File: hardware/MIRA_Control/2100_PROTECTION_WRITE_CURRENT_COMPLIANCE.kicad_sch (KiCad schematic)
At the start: 66 parts, among them U2100 ADG5408, U2101 OPA197, U2103 ADG5409, U2104 INA821, U2105 OPA4197, U2106 OPA4197, U2107 OPA4197, U2108 SN74LVC1G04, U2109 INA821

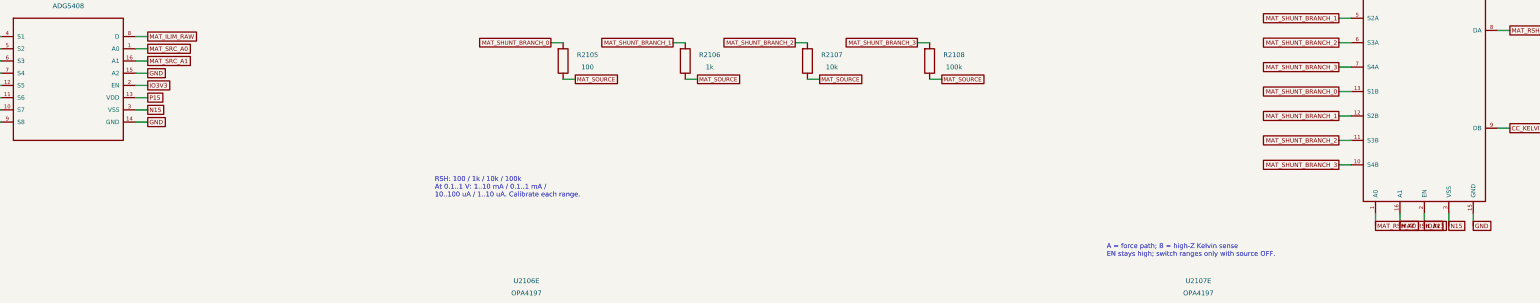
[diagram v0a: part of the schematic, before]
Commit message: Select Samtec inter-board connectors and resolve analog VSS ERC warnings
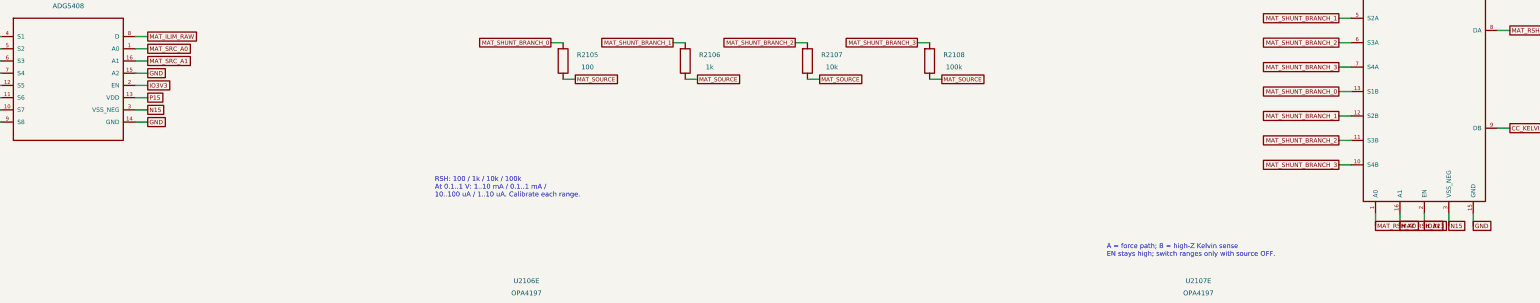
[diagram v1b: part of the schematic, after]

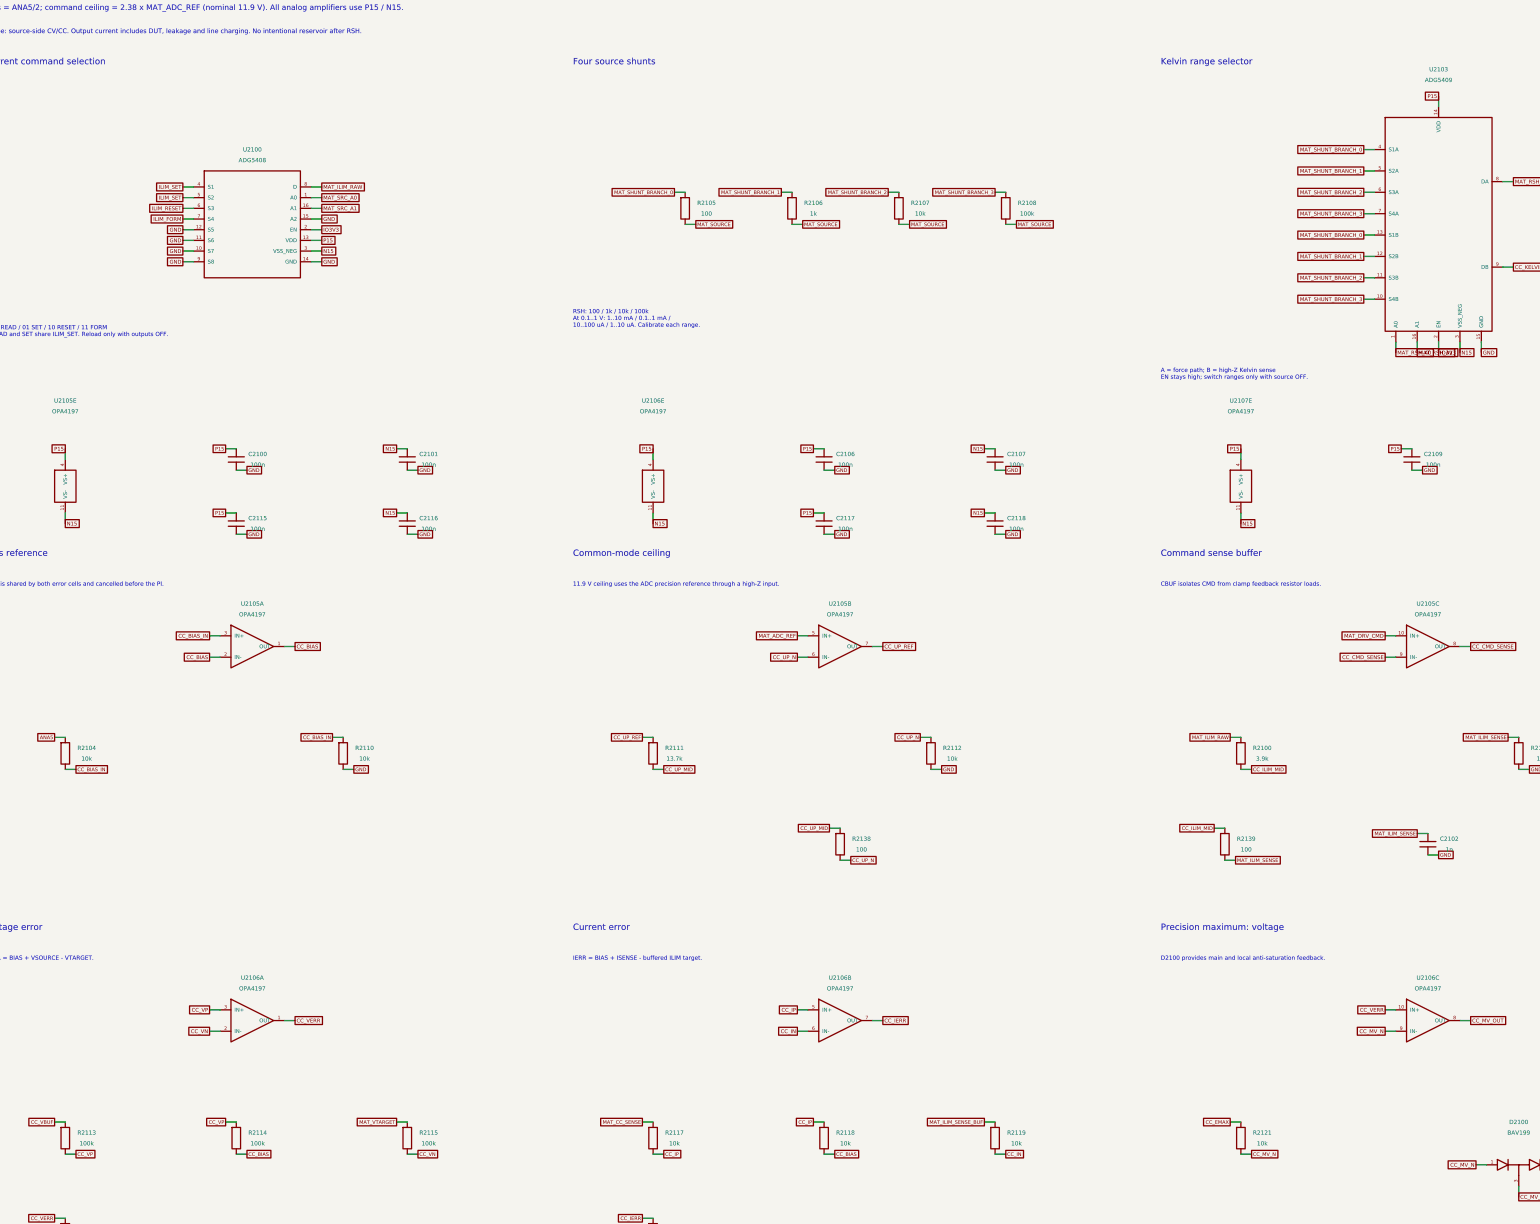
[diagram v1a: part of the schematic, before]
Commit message: Protect unpowered signal domains and qualify local supplies; retain startup and fault interlocks
MIRA-Startup-Patch: 7ffae17756ebcf923eff1212bb1aade8fbdfae03a9ca8ecebc69d3da3d3b4ba2
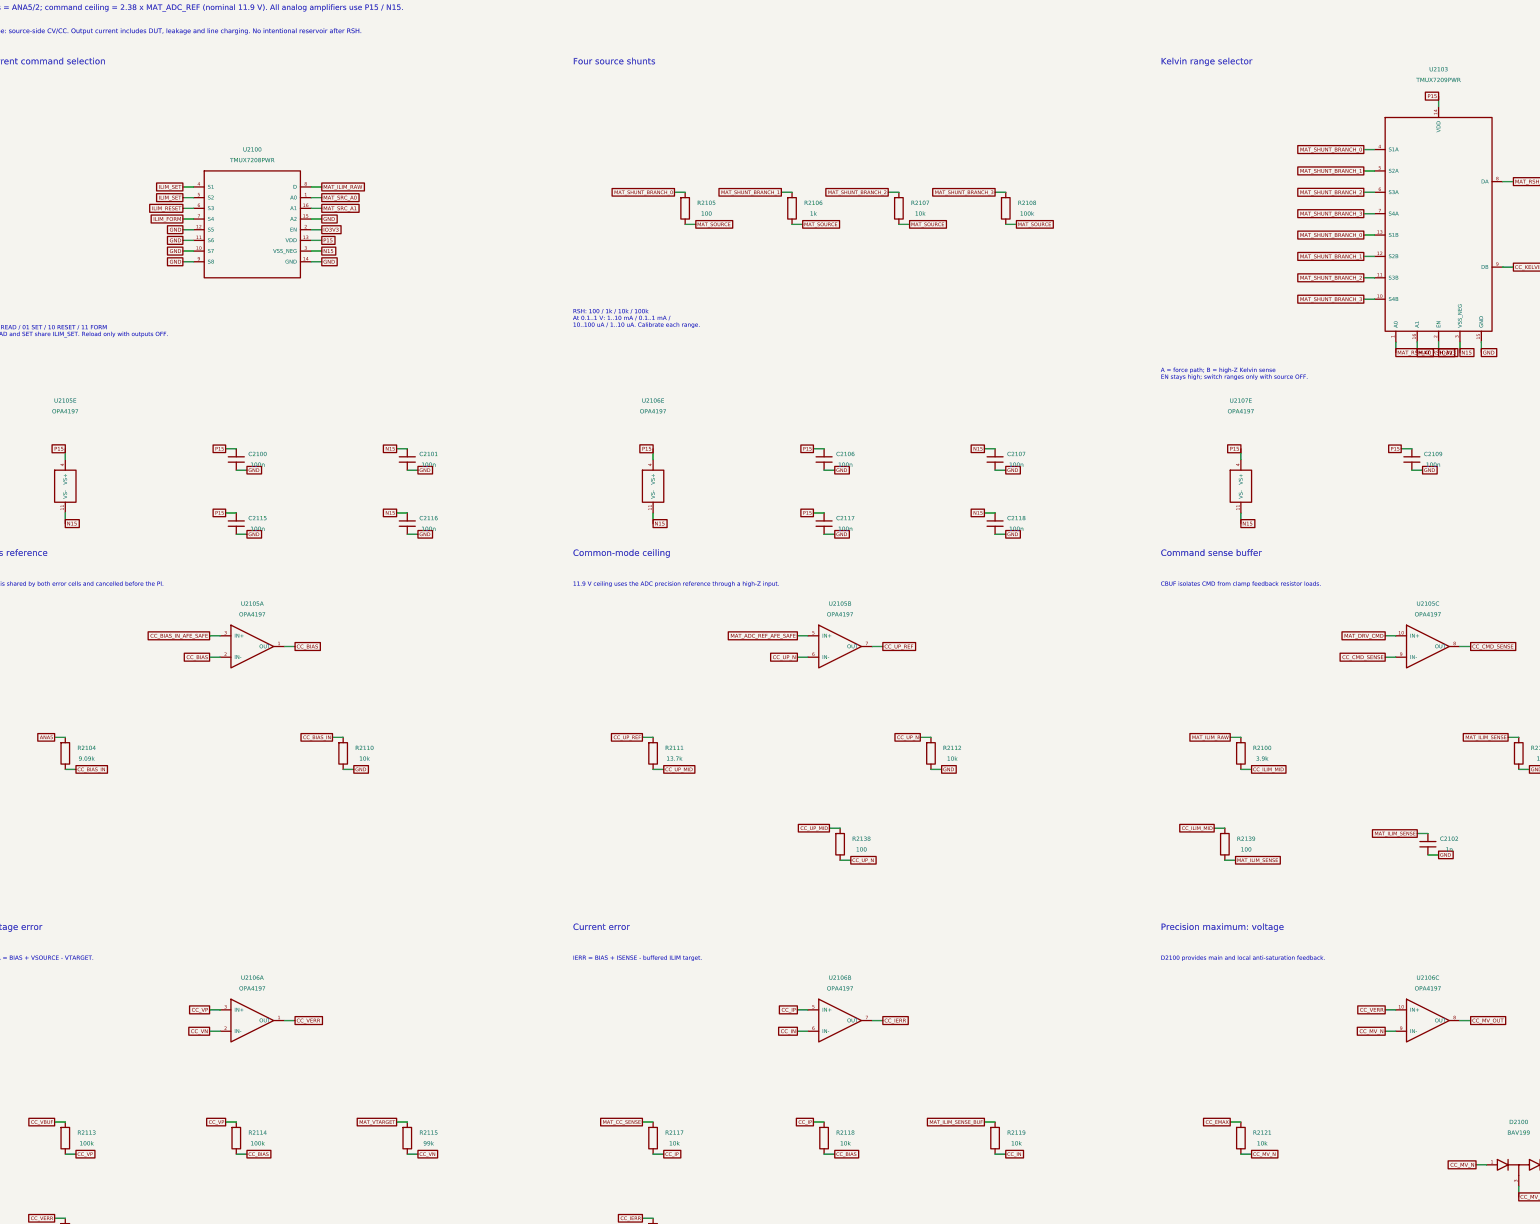
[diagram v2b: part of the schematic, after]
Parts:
- R2104: value 10k -> 9.09k; MPN RT0603BRD0710KL -> ERJ-2RKF9091X
- R2115: value 100k -> 99k; MPN RT0603BRD07100KL -> ERA-2AEB9902X
- U2100: value ADG5408 -> TMUX7208PWR; symbol MIRA_RevA:ADG5408_MIRA_MAT -> MIRA_RevA:TMUX7208PWR_SIGNAL_MIRA; MPN ADG5408BRUZ -> TMUX7208PWR; Manufacturer Analog Devices -> Texas Instruments
- U2103: value ADG5409 -> TMUX7209PWR; symbol MIRA_RevA:ADG5409_CC_MIRA -> MIRA_RevA:TMUX7209PWR_SIGNAL_MIRA; MPN ADG5409BRUZ -> TMUX7209PWR; Manufacturer Analog Devices -> Texas Instruments
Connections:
- net CC_BIAS_IN: no longer U2105.3 (IN+)
- net MAT_ADC_REF renamed MAT_ADC_REF_AFE_SAFE
- new net CC_BIAS_IN_AFE_SAFE: U2105.3 (IN+)

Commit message: MIRA.05: analog requirements and schematic fixes
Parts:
- R2104: MPN ERJ-2RKF9091X -> RT0603BRD079K09L
- R2111: value 13.7k -> 10k; MPN RT0603BRD0713K7L -> RT0603BRD0710KL
- R2115: value 99k -> 100k; MPN ERA-2AEB9902X -> RT0603BRD07100KL
- R2116: value 100k -> 101k; MPN RT0603BRD07100KL -> TNPW0603101KBEEA; Manufacturer YAGEO -> Vishay
- U2109: value INA821 -> INA149AIDR; symbol MIRA_RevA:INA821_CC_MIRA -> MIRA_RevA:INA149_AW_MIRA; MPN INA821IDR -> INA149AIDR
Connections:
- net CC_AW: now also U2109.6 (OUT); no longer U2109.7 (OUT)
- net CC_CMD_SENSE: now also U2109.2 (-IN)
- net GND: now also U2109.1 (REFB), U2109.5 (REFA); no longer U2109.6 (REF)
- net MAT_DRV_CMD: no longer U2109.1 (IN-)
- net MAT_PI_RAW: now also U2109.3 (+IN); no longer U2109.4 (IN+)
- net N15: now also U2109.4 (VSS_NEG); no longer U2109.5 (VS-)
- net P15: now also U2109.7 (V+); no longer U2109.8 (VS+)
- no-connect marks 6 -> 5
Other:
- note added: "10.05 V ceiling uses the ADC precision reference through a high-Z input."
- note added: "Bias is approximately ANA5/2 (loaded divider); command ceiling = 2.01 x MAT_ADC_REF (nominal 10.05 V). All analog amplifiers use P15/N15."
- note added: "Ceiling = 2.01 x MAT_ADC_REF; actual output depends on load drop."
- note added: "Current sense / high-CM anti-windup"
- note added: "Lower limit 0 V; upper command nominal 10.05 V. CBUF isolates clamp feedback. INA149 back-calculation measures RAW - buffered CMD."
- note added: "R2115=100k and R2116=101k include the 1k guard series path. Nominal CV gain is about 0.99976, including target guard loading. Driver feeds the source-OFF SPDT; calibrate the complete path."
- note added: "RSH: 100 / 1k / 10k / 100k; all four in service READ/WRITE. Initial profile uses 0.08..0.8 V sense; standard current 10 uA..8 mA. Nominal full-DAC capability is about 10 mA; calibrate zero/gain."
- note added: "Scope: source-side CV/CC includes DUT, leakage and charging. Microsecond pulse accuracy and transient peak current are NOT qualified; see MIRA.05."
- note removed: "11.9 V ceiling uses the ADC precision reference through a high-Z input."
- note removed: "Bias = ANA5/2; command ceiling = 2.38 x MAT_ADC_REF (nominal 11.9 V). All analog amplifiers use P15 / N15."
- note removed: "Ceiling = 2.38 x MAT_ADC_REF; actual output depends on load drop."
- note removed: "Current and back-calculation sense"
- note removed: "Lower limit 0 V; upper command nominal 11.9 V. CBUF isolates clamp feedback. INA821 back-calculation measures RAW - CMD without loading CMD."
- note removed: "RSH: 100 / 1k / 10k / 100k At 0.1..1 V: 1..10 mA / 0.1..1 mA / 10..100 uA / 1..10 uA. Calibrate each range."
- note removed: "Scope: source-side CV/CC. Output current includes DUT, leakage and line charging. No intentional reservoir after RSH."
- note removed: "Voltage input is high-Z. Driver feeds source-OFF SPDT on sheet1600."
